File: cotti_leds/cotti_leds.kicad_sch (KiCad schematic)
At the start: 0 parts

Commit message: feat: cotti_leds schematic
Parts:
- added D5: Blue Vf=3.3V If=0-20mA, symbol Device:LED
- added D6: Orange Vf=2V If=0-20mA, symbol Device:LED
- added D7: Red Vf=2V If=0-20mA, symbol Device:LED
- added D8: Yellow-Green Vf=2V If=0-20mA, symbol Device:LED
- added D9: Ambar Vf=2V If=0-20mA, symbol Device:LED
- added H1, H2, H3, H4: M2, symbol Mechanical:MountingHole
- added J1: Pmod GPIO 1x06 pin, Pmod:Pmod_1x06_pin, symbol Pmod:pmod_gpio_1x06_pin
- added JP1: IO1 L/H, symbol Jumper:Jumper_3_Bridged12
- added JP2: IO2 L/H, symbol Jumper:Jumper_3_Bridged12
- added JP3: IO3 L/H, symbol Jumper:Jumper_3_Bridged12
- added JP4: IO4 L/H, symbol Jumper:Jumper_3_Bridged12
- added R1, R2, R3, R4: 100R, symbol Device:R_US
- added R5, R6, R7, R8: 180R, symbol Device:R_US
- added SW1: SW_4PDT, Cotti_misc:SW_4PDT, symbol Cotti_misc:SW_4PDT
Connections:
- new net: D5.1 (K), D6.2 (A), D9.1 (K)
- new net: D5.2 (A), D7.2 (A), D9.2 (A)
- new net: D7.1 (K), D8.2 (A)
- new net: J1.2 (IO2/PWM), R2.1
- new net: D6.1 (K), D8.1 (K)
- new net: J1.4 (IO4), R4.1
- new net: J1.1 (IO1), R1.1
- new net: R8.1, SW1.12 (C)
- new net: R5.1, SW1.3 (C)
- new net: R6.1, SW1.6 (C)
- new net: R7.1, SW1.9 (C)
- new net: J1.3 (IO3), R3.1
- new net GND: J1.5 (GND), SW1.13 (GND), SW1.14 (GND)
- new net VCC: J1.6 (VCC), SW1.11 (B), SW1.2 (B), SW1.5 (B), SW1.8 (B)
- new net io1: JP1.2 (C), R1.2
- new net io1_H: JP1.1 (A)
- new net io1_L: JP1.3 (B)
- new net io2: JP2.2 (C), R2.2
- new net io2_H: JP2.1 (A)
- new net io2_L: JP2.3 (B)
- new net io3: JP3.2 (C), R3.2
- new net io3_H: JP3.1 (A)
- new net io3_L: JP3.3 (B)
- new net io4: JP4.2 (C), R4.2
- new net io4_H: JP4.1 (A)
- new net io4_L: JP4.3 (B)
- new net vcc1: R5.2, SW1.1 (A)
- new net vcc2: R6.2, SW1.4 (A)
- new net vcc3: R7.2, SW1.7 (A)
- new net vcc4: R8.2, SW1.10 (A)
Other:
- added sheet LED_frontend (led_frontend.kicad_sch)
- added sheet LED_frontend1 (led_frontend.kicad_sch)
- added sheet LED_frontend2 (led_frontend.kicad_sch)
- added sheet LED_frontend3 (led_frontend.kicad_sch)
- note added: "3.3V / 5V Selection"
- note added: "Alternative LEDS (not included in PCB)"
- note added: "Choosing high-asserted or low-asserted GPIO"
- note added: "LED frontends"
- note added: "Mounting Holes"
- note added: "PMOD GPIO"

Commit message: feat: cotti_leds first version
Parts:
- removed H1, H2, H3, H4: M2, symbol Mechanical:MountingHole
- added H5, H6, H7, H8: Jmp shunt, Cotti_misc:Empty_footprint, symbol Cotti_misc:Jumper_shunt_open_top
- D5, D6, D7, D8, D9: footprint (none) -> LED_SMD:LED_0603_1608Metric_Pad1.05x0.95mm_HandSolder
- JP1, JP2, JP3, JP4: footprint (none) -> Connector_PinHeader_2.54mm:PinHeader_1x03_P2.54mm_Vertical; Digikey (none) -> https://www.digikey.com/en/products/detail/adam-tech/PH1-03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; Digikey P/N (none) -> 2057-PH1-03-UA-ND; Mfr. (none) -> Adam Tech; Mfr. P/N (none) -> PH1-03-UA
- R1, R2, R3, R4: value 100R -> 200R; footprint (none) -> Resistor_SMD:R_0805_2012Metric_Pad1.20x1.40mm_HandSolder; Digikey (none) -> https://www.digikey.com/en/products/detail/stackpole-electr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; Digikey P/N (none) -> RMCF0805JT200RCT-ND; Mfr. (none) -> Stackpole Electronics Inc; Mfr. P/N (none) -> RMCF0805JT200R
- R5, R6, R7, R8: value 180R -> 200R; footprint (none) -> Resistor_SMD:R_0805_2012Metric_Pad1.20x1.40mm_HandSolder; Digikey (none) -> https://www.digikey.com/en/products/detail/stackpole-electr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; Digikey P/N (none) -> RMCF0805JT200RCT-ND; Mfr. (none) -> Stackpole Electronics Inc; Mfr. P/N (none) -> RMCF0805JT200R
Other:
- note removed: "Mounting Holes"

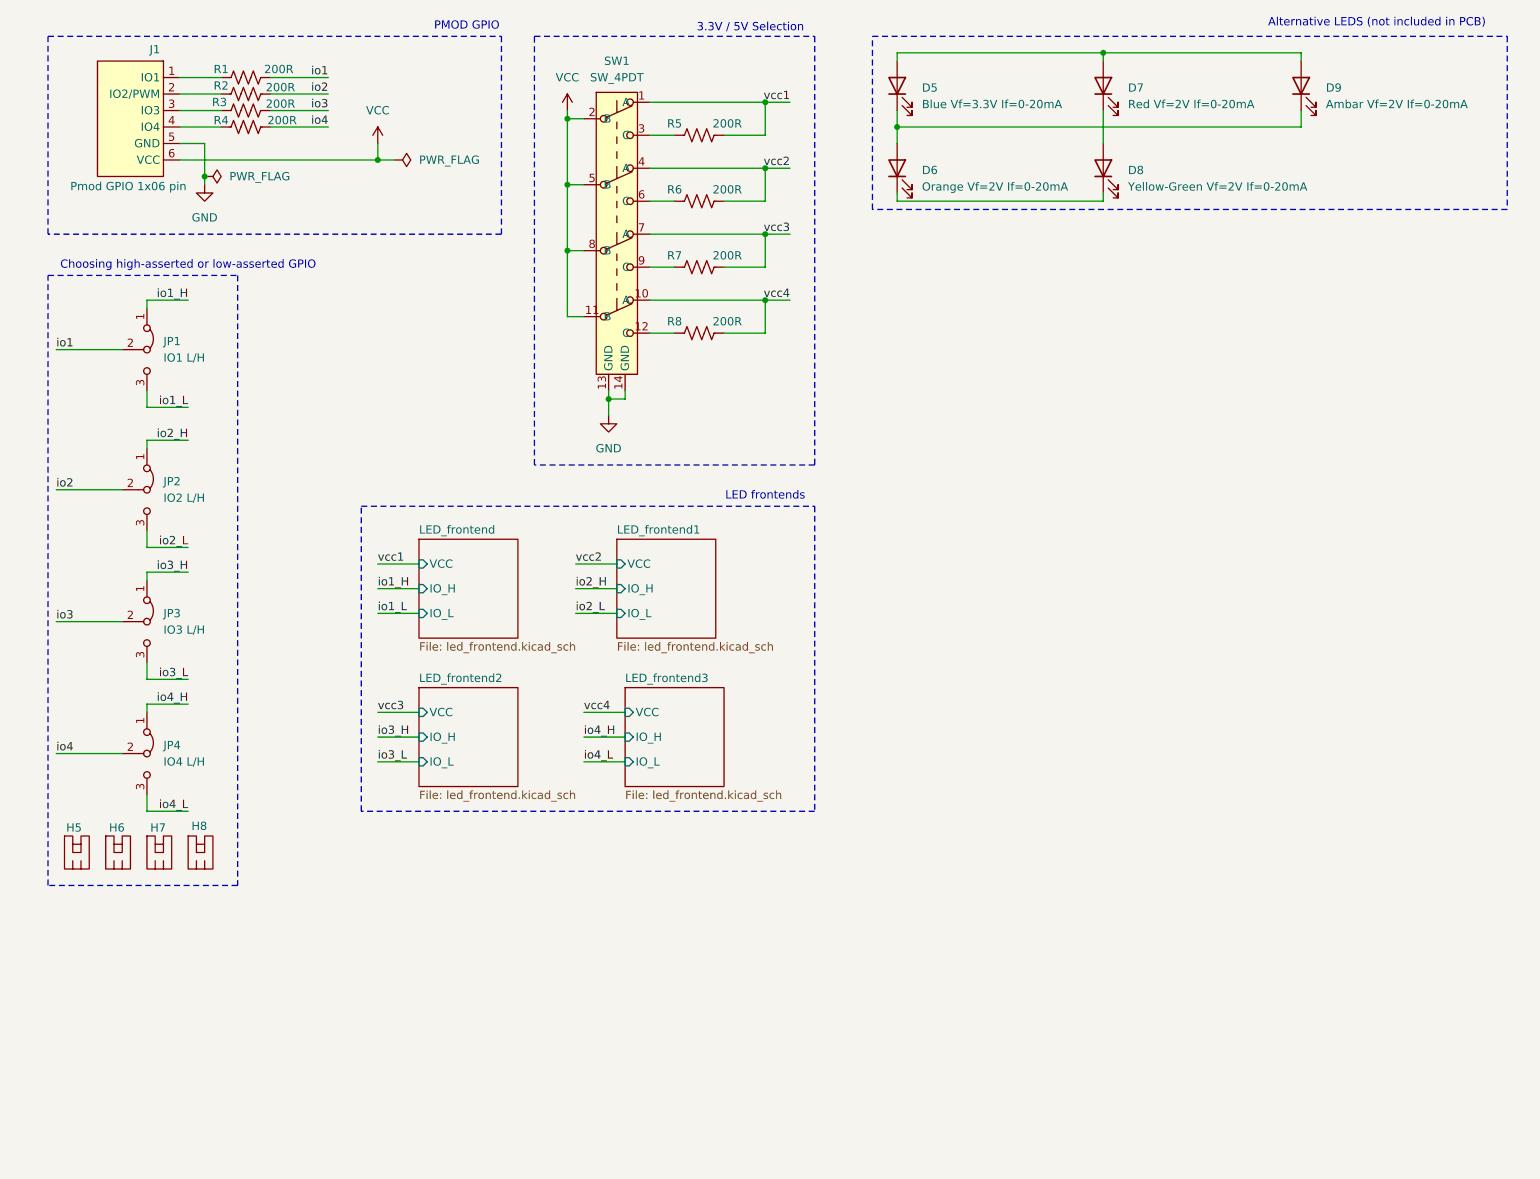
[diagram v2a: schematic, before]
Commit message: feat: cotti leds with new library format
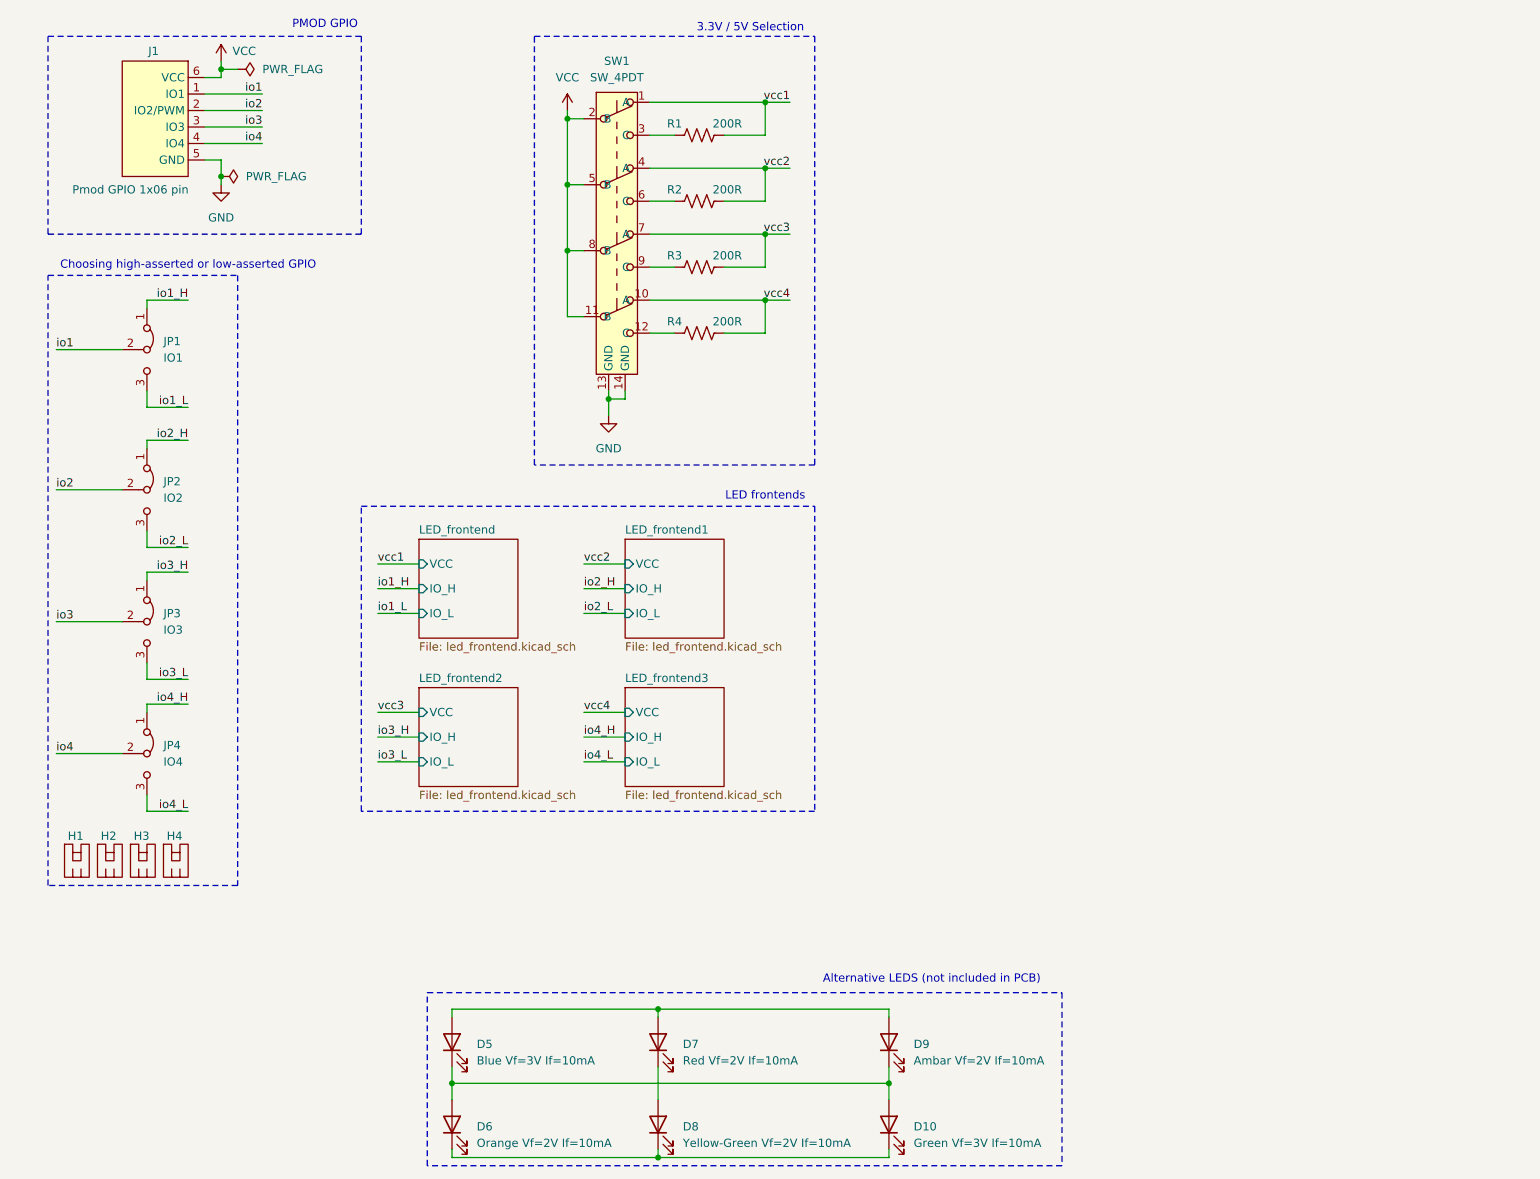
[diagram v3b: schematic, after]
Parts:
- removed D5: Blue Vf=3.3V If=0-20mA, LED_SMD:LED_0603_1608Metric_Pad1.05x0.95mm_HandSolder, symbol Device:LED
- removed D6: Orange Vf=2V If=0-20mA, LED_SMD:LED_0603_1608Metric_Pad1.05x0.95mm_HandSolder, symbol Device:LED
- removed D7: Red Vf=2V If=0-20mA, LED_SMD:LED_0603_1608Metric_Pad1.05x0.95mm_HandSolder, symbol Device:LED
- removed D8: Yellow-Green Vf=2V If=0-20mA, LED_SMD:LED_0603_1608Metric_Pad1.05x0.95mm_HandSolder, symbol Device:LED
- removed D9: Ambar Vf=2V If=0-20mA, LED_SMD:LED_0603_1608Metric_Pad1.05x0.95mm_HandSolder, symbol Device:LED
- removed H5, H6, H7, H8: Jmp shunt, Cotti_misc:Empty_footprint, symbol Cotti_misc:Jumper_shunt_open_top
- removed J1: Pmod GPIO 1x06 pin, Pmod:Pmod_1x06_pin, symbol Pmod:pmod_gpio_1x06_pin
- removed JP1: IO1 L/H, Connector_PinHeader_2.54mm:PinHeader_1x03_P2.54mm_Vertical, symbol Jumper:Jumper_3_Bridged12
- removed JP2: IO2 L/H, Connector_PinHeader_2.54mm:PinHeader_1x03_P2.54mm_Vertical, symbol Jumper:Jumper_3_Bridged12
- removed JP3: IO3 L/H, Connector_PinHeader_2.54mm:PinHeader_1x03_P2.54mm_Vertical, symbol Jumper:Jumper_3_Bridged12
- removed JP4: IO4 L/H, Connector_PinHeader_2.54mm:PinHeader_1x03_P2.54mm_Vertical, symbol Jumper:Jumper_3_Bridged12
- removed R1, R2, R3, R4: 200R, Resistor_SMD:R_0805_2012Metric_Pad1.20x1.40mm_HandSolder, symbol Device:R_US
- removed SW1: SW_4PDT, Cotti_misc:SW_4PDT, symbol Cotti_misc:SW_4PDT
- added D10: Green Vf=3V If=10mA, LED_SMD:LED_0603_1608Metric_Pad1.05x0.95mm_HandSolder, symbol cotti_leds:LED_Green_SMD
- added D5: Blue Vf=3V If=10mA, LED_SMD:LED_0603_1608Metric_Pad1.05x0.95mm_HandSolder, symbol cotti_leds:LED_Blue_SMD
- added D6: Orange Vf=2V If=10mA, LED_SMD:LED_0603_1608Metric_Pad1.05x0.95mm_HandSolder, symbol cotti_leds:LED_Orange_SMD
- added D7: Red Vf=2V If=10mA, LED_SMD:LED_0603_1608Metric_Pad1.05x0.95mm_HandSolder, symbol cotti_leds:LED_Red_SMD
- added D8: Yellow-Green Vf=2V If=10mA, LED_SMD:LED_0603_1608Metric_Pad1.05x0.95mm_HandSolder, symbol cotti_leds:LED_Yellow_Green_SMD
- added D9: Ambar Vf=2V If=10mA, LED_SMD:LED_0603_1608Metric_Pad1.05x0.95mm_HandSolder, symbol cotti_leds:LED_Ambar_SMD
- added H1, H2, H3, H4: Jmp shunt, cotti_footprints:Empty_footprint, symbol cotti_connectors:Jumper_shunt_open_top
- added J1: Pmod GPIO 1x06 pin, cotti_footprints:Pmod_1x06_pin, symbol cotti_pmod:pmod_gpio_1x06_pin
- added JP1: IO1, Connector_PinHeader_2.54mm:PinHeader_1x03_P2.54mm_Vertical, symbol cotti_connectors:Jumper_3_Bridged12
- added JP2: IO2, Connector_PinHeader_2.54mm:PinHeader_1x03_P2.54mm_Vertical, symbol cotti_connectors:Jumper_3_Bridged12
- added JP3: IO3, Connector_PinHeader_2.54mm:PinHeader_1x03_P2.54mm_Vertical, symbol cotti_connectors:Jumper_3_Bridged12
- added JP4: IO4, Connector_PinHeader_2.54mm:PinHeader_1x03_P2.54mm_Vertical, symbol cotti_connectors:Jumper_3_Bridged12
- added SW1: SW_4PDT, cotti_footprints:SW_4PDT, symbol cotti_switch:SW_4PDT
- R1: renamed from R5; Digikey P/N RMCF0805JT200RCT-ND -> (none)
- R2: renamed from R6; Digikey P/N RMCF0805JT200RCT-ND -> (none)
- R3: renamed from R7; Digikey P/N RMCF0805JT200RCT-ND -> (none)
- R4: renamed from R8; Digikey P/N RMCF0805JT200RCT-ND -> (none)
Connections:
- net GND: now also J1.5 (GND), SW1.13 (GND), SW1.14 (GND)
- net VCC: now also J1.6 (VCC), SW1.11 (B), SW1.2 (B), SW1.5 (B), SW1.8 (B)
- net io1: now also J1.1 (IO1), JP1.2 (C)
- net io1_H: now also JP1.1 (A)
- net io1_L: now also JP1.3 (B)
- net io2: now also J1.2 (IO2/PWM), JP2.2 (C)
- net io2_H: now also JP2.1 (A)
- net io2_L: now also JP2.3 (B)
- net io3: now also J1.3 (IO3), JP3.2 (C)
- net io3_H: now also JP3.1 (A)
- net io3_L: now also JP3.3 (B)
- net io4: now also J1.4 (IO4), JP4.2 (C)
- net io4_H: now also JP4.1 (A)
- net io4_L: now also JP4.3 (B)
- net vcc1: now also SW1.1 (A)
- net vcc2: now also SW1.4 (A)
- net vcc3: now also SW1.7 (A)
- net vcc4: now also SW1.10 (A)
- net at R4.1: now also SW1.12 (C)
- net at R1.1: now also SW1.3 (C)
- net at R2.1: now also SW1.6 (C)
- net at R3.1: now also SW1.9 (C)
- new net: D10.1 (K), D6.1 (K), D8.1 (K)
- new net: D10.2 (A), D5.1 (K), D6.2 (A), D9.1 (K)
- new net: D7.1 (K), D8.2 (A)
- new net: D5.2 (A), D7.2 (A), D9.2 (A)

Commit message: feat: cotti leds gerber files
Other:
- company: (none) -> Cotti
- title: (none) -> Led module
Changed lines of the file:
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@@
 	(generator_version "9.0")
 	(paper "A4")
+	(title_block
+		(title "Led module")
+		(date "2026-01-17")
+		(rev "0.0")
+		(company "Cotti")
+	)
 	(rectangle
 		(start 67.31 93.98)
